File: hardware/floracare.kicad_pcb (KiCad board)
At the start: 2 copper layers, 100 x 100 mm, 17 parts, among them J1 USB_C_Receptacle_USB2.0_14P, J2 Conn_01x04_Socket, J4 Conn_01x04_Socket, J5 Conn_01x14_Socket, J6 Conn_01x05_Socket, U1 AMS1117-3.3, U2 ESP32-S3-WROOM-1

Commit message: Update global pcb
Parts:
- removed J1: USB_C_Receptacle_USB2.0_14P, Connector_USB:USB_C_Receptacle_HCTL_HC-TYPE-C-16P-01A
- added J3: USB_C_Receptacle_USB2.0_16P, Connector_USB:USB_C_Receptacle_HCTL_HC-TYPE-C-16P-01A, F.Cu at (235.9, 106.0)
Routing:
- net +3V3: track 21.7 -> 154.0 mm, vias 0 -> 2
- net DATA+: track 50.8 -> 37.2 mm
- net Net-(J3-CC2): track 7.15 -> 8.87 mm
- net Net-(J3-CC1): track 7.15 -> 8.87 mm
- net +5V: track 26.3 -> 27.4 mm, vias 0 -> 2
- net DATA-: track 36.4 -> 35.8 mm
- added copper zone on B.Cu, net GND
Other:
- board text added: "3.5{dblquote} TFT SPI 480*320 SCREEN"

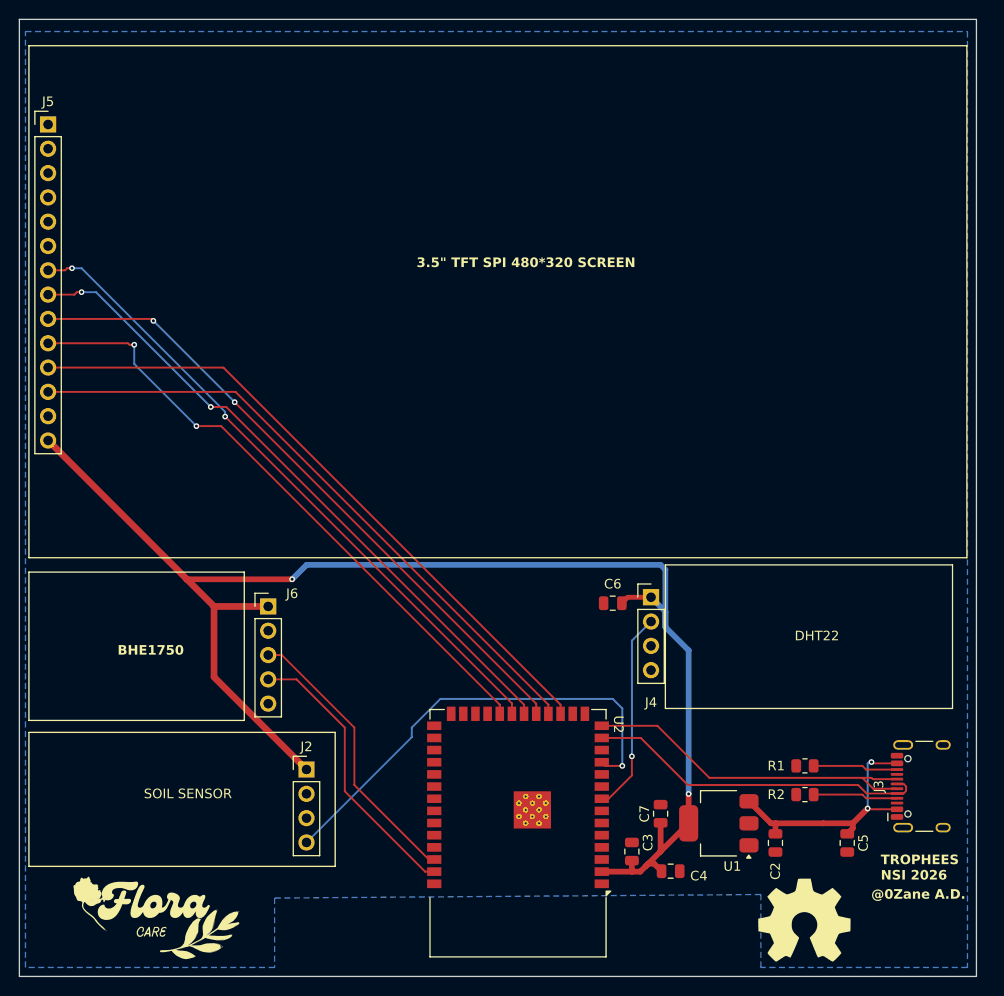
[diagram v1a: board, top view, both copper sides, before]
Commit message: Fixing size hole problem and mass plan [ ERC 9 ERRORS ]
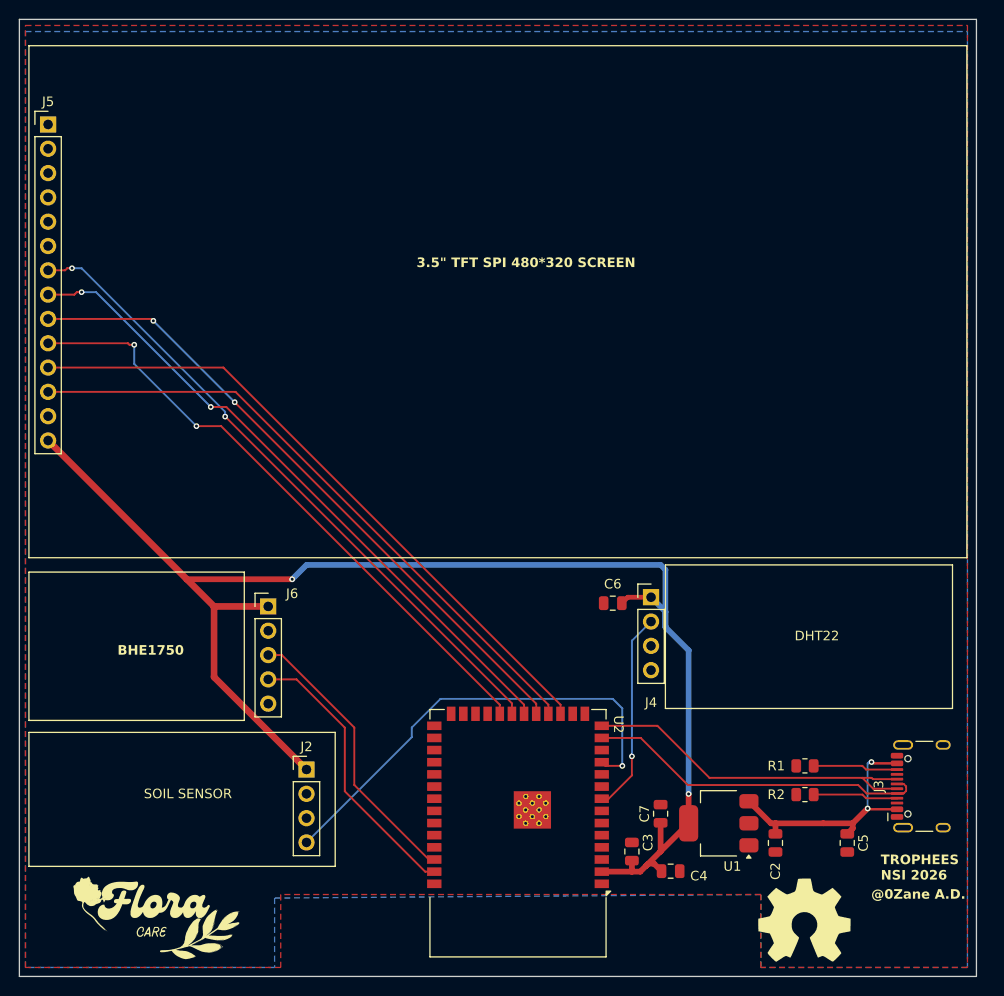
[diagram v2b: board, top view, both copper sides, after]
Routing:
- added copper zone on F.Cu, net GND
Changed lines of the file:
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@@
 			(at -2.9 1.76 270)
 			(size 0.6 0.6)
-			(drill 0.2)
+			(drill 0.3)
 			(property pad_prop_heatsink)
 			(layers "*.Cu" "F.Mask")
@@
 			(at -2.9 3.16 180)
 			(size 0.6 0.6)
-			(drill 0.2)
+			(drill 0.3)
 			(property pad_prop_heatsink)
 			(layers "*.Cu" "F.Mask")
@@
 			(at -2.2 1.06 180)
 			(size 0.6 0.6)
-			(drill 0.2)
+			(drill 0.3)
 			(property pad_prop_heatsink)
 			(layers "*.Cu" "F.Mask")
@@
 			(at -2.2 2.46 180)
 			(size 0.6 0.6)
-			(drill 0.2)
+			(drill 0.3)
 			(property pad_prop_heatsink)
 			(layers "*.Cu" "F.Mask")
@@
 			(at -2.2 3.86 180)
 			(size 0.6 0.6)
-			(drill 0.2)
+			(drill 0.3)
 			(property pad_prop_heatsink)
 			(layers "*.Cu" "F.Mask")
@@
 			(at -1.5 1.76 180)
 			(size 0.6 0.6)
-			(drill 0.2)
+			(drill 0.3)
 			(property pad_prop_heatsink)
 			(layers "*.Cu" "F.Mask")
@@
 			(at -1.5 3.16 180)
 			(size 0.6 0.6)
-			(drill 0.2)
+			(drill 0.3)
 			(property pad_prop_heatsink)
 			(layers "*.Cu" "F.Mask")
@@
 			(at -0.8 1.06 180)
 			(size 0.6 0.6)
-			(drill 0.2)
+			(drill 0.3)
 			(property pad_prop_heatsink)
 			(layers "*.Cu" "F.Mask")
@@
 			(at -0.8 2.46 180)
 			(size 0.6 0.6)
-			(drill 0.2)
+			(drill 0.3)
 			(property pad_prop_heatsink)
 			(layers "*.Cu" "F.Mask")
@@
 			(at -0.8 3.86 180)
 			(size 0.6 0.6)
-			(drill 0.2)
+			(drill 0.3)
 			(property pad_prop_heatsink)
 			(layers "*.Cu" "F.Mask")
@@
 			(at -0.1 1.76 180)
 			(size 0.6 0.6)
-			(drill 0.2)
+			(drill 0.3)
 			(property pad_prop_heatsink)
 			(layers "*.Cu" "F.Mask")
@@
 			(at -0.1 3.16 180)
 			(size 0.6 0.6)
-			(drill 0.2)
+			(drill 0.3)
 			(property pad_prop_heatsink)
 			(layers "*.Cu" "F.Mask")
@@
 		(start 232.12 103.585)
 		(end 229.585 103.585)
-		(width 0.2)
+		(width 0.26)
 		(layer "F.Cu")
 		(net 3)
@@
 		(start 232.12 108.385)
 		(end 229.135 108.385)
-		(width 0.2)
+		(width 0.26)
 		(layer "F.Cu")
 		(net 3)
@@
 	)
 	(zone
+		(net 2)
+		(net_name "GND")
+		(layer "F.Cu")
+		(hatch edge 0.5)
+		(priority 1)
+		(connect_pads
+			(clearance 0.5)
+		)
+		(min_thickness 0.25)
+		(filled_areas_thickness no)
+		(fill yes
+			(thermal_gap 0.5)
+			(thermal_bridge_width 0.5)
+		)
+		(polygon
+			(pts
+				(xy 141.055 26.485) (xy 239.48 26.485) (xy 239.48 124.91) (xy 217.89 124.91) (xy 217.89 117.29)
+				(xy 167.725 117.29) (xy 167.725 124.91) (xy 141.055 124.91)
+			)
+		)
+	)
+	(zone
